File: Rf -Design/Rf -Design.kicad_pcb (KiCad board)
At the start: 4 copper layers, 39.8 x 17.2 mm, 39 parts, among them J1 USB_B_Micro, J2 SMA, J3 SWD, U1 XC6206PxxxMR, U2 USBLC6-2SC6, U3 STM32L432KBUx, U4 nRF24L01P, Y1 Crystal_GND23

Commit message: Update README.md
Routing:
- net +3V3: track 4.99 -> 11.5 mm

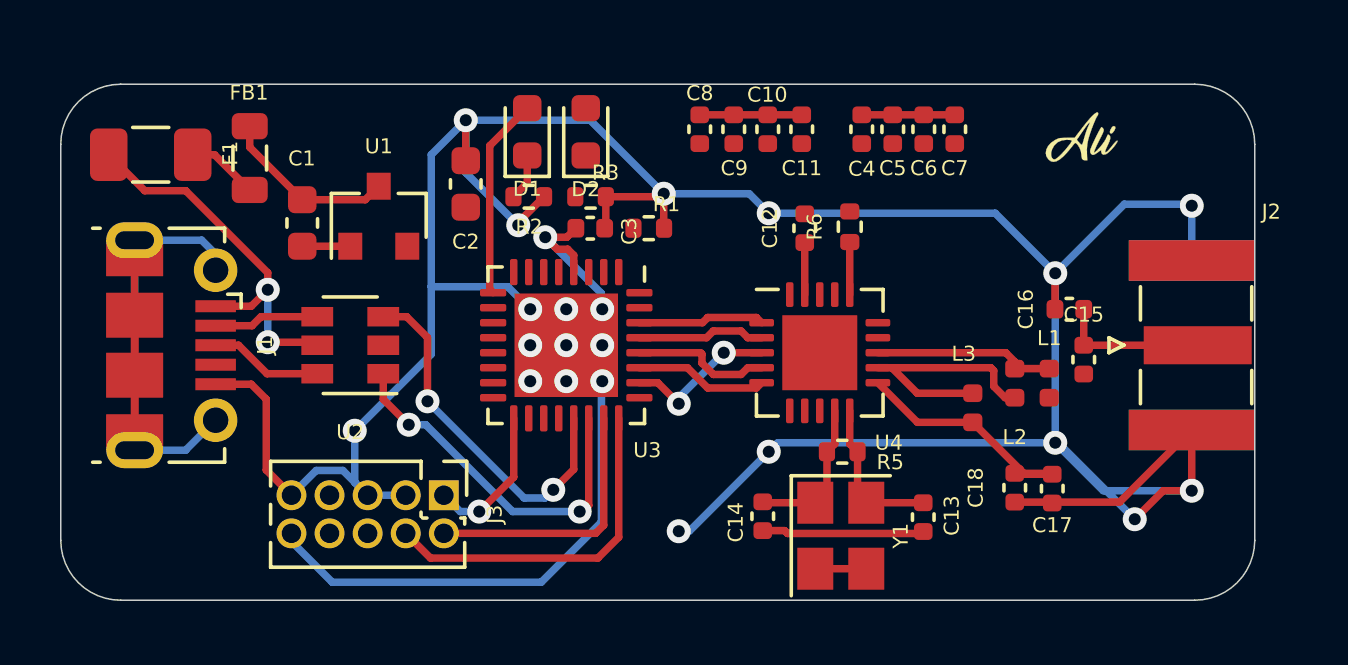
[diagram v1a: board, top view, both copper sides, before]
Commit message: Route tracks are arranged
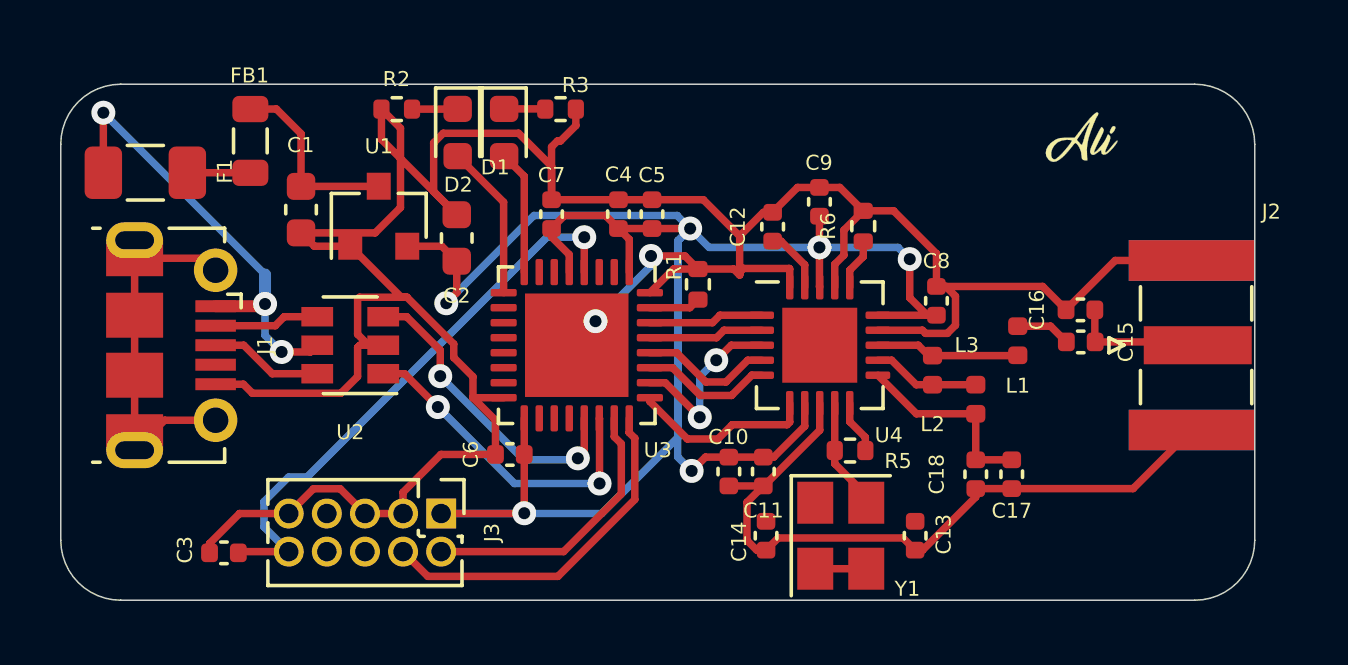
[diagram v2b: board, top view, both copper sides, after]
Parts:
- moved C6 17.5 mm to (110.4, 93.7), turned to 180 degrees
- moved C3 16.3 mm to (100.8, 97.0), turned to 180 degrees
- moved C7 13.7 mm to (111.8, 85.7), turned to 90 degrees
- moved C10 11.5 mm to (117.7, 94.3)
- moved C11 11.5 mm to (118.8, 94.3)
- moved C8 9.75 mm to (124.6, 88.6), turned to 90 degrees
- moved C4 8.59 mm to (114.0, 85.7), turned to 90 degrees
- moved C5 8.51 mm to (115.1, 85.7), turned to 90 degrees
- moved R2 5.28 mm to (106.6, 82.2), turned to 180 degrees
- moved C9 3.74 mm to (120.7, 85.3), turned to 90 degrees
- moved R3 3.09 mm to (112.1, 82.2)
- moved L2 2.77 mm to (124.5, 90.9)
- moved D2 2.72 mm to (110.2, 83.0), turned to 270 degrees
- moved R1 2.49 mm to (116.6, 88.1), turned to 90 degrees
- moved D1 2.32 mm to (108.6, 83.0), turned to 270 degrees
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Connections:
- Y1 pad 1: NRF_XC2 -> NRF_XC1
- Y1 pad 4: NRF_XC1 -> NRF_XC2
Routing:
- net +3V3: track 11.5 -> 71.3 mm, vias 1 -> 6
- net Net-(J1-Pad6): track 24.4 -> 13.0 mm
- net GND: track 117.4 -> 128.1 mm, vias 21 -> 2
- net NRF_IRQ: track 0.00 -> 6.16 mm
- net NRST: track 25.2 -> 19.2 mm
- net NRF_ANT1: track 8.33 -> 3.60 mm
- net Net-(D2-Pad2): track 0.00 -> 4.14 mm
- net NRF_XC1: track 5.19 -> 2.34 mm
- net +5V: track 12.9 -> 15.5 mm, vias 2 -> 3
- net Net-(C15-Pad1): track 0.00 -> 1.84 mm
- net NRF_VDD_PA: track 8.34 -> 6.53 mm
- net USB_D-: track 12.2 -> 10.4 mm
- net Net-(R1-Pad1): track 0.00 -> 1.71 mm
- net Net-(D1-Pad2): track 6.71 -> 5.19 mm
- net Net-(D2-Pad1): track 0.00 -> 1.37 mm
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- removed copper zone on In2.Cu, net +3V3

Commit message: The texts on the f-silk layer are fixed
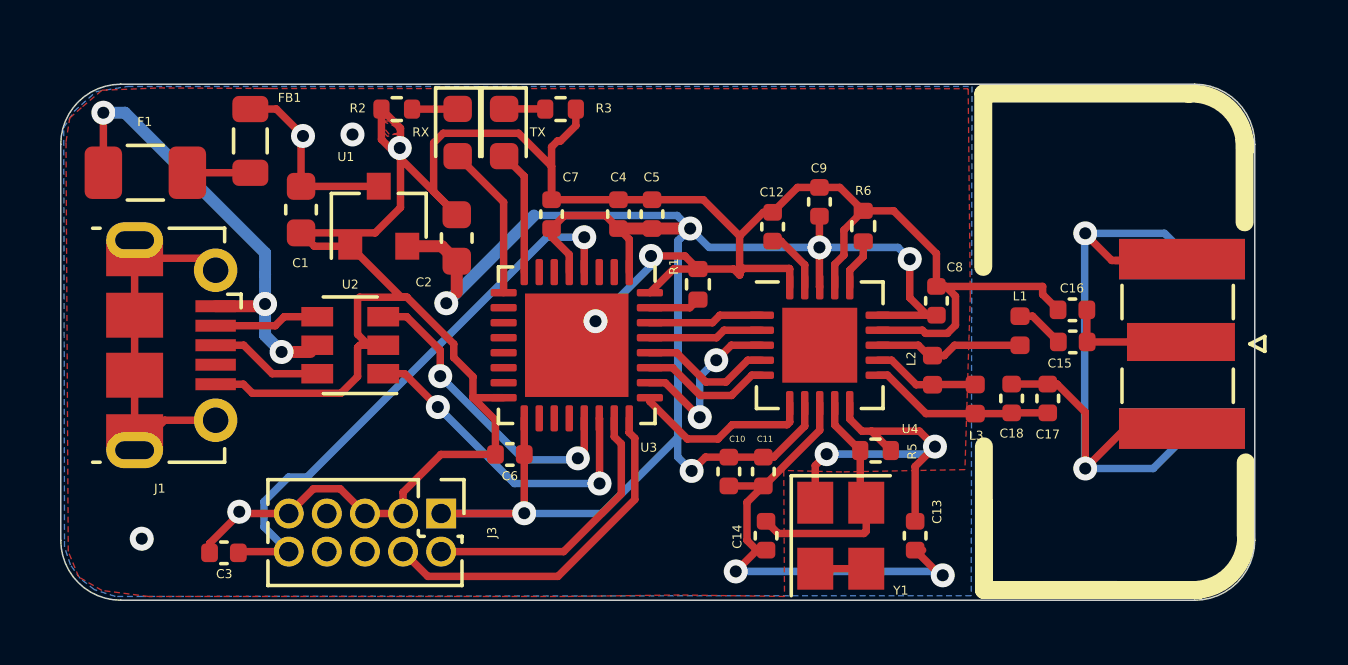
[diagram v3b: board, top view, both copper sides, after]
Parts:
- G***: moved to B.Cu
- moved G*** 12.0 mm to (117.5, 83.0)
- moved C17 2.80 mm to (128.3, 91.9), turned to 90 degrees
- moved C18 2.79 mm to (127.1, 91.9), turned to 90 degrees
- moved R5 0.85 mm to (122.6, 93.6)
- moved L1 0.34 mm to (127.4, 89.6)
- moved J2 0.33 mm to (132.8, 90.1), turned to 270 degrees
- moved C15 0.27 mm to (129.1, 90.0)
- moved C16 0.27 mm to (129.1, 88.9)
- renumbered D1 to RX, D2 to TX
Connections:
- C1 pad 1: Net-(C1-Pad1) -> GND
- FB1 pad 1: Net-(C1-Pad1) -> GND
- U1 pad 3: Net-(C1-Pad1) -> GND
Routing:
- net GND: track 128.1 -> 154.1 mm, vias 2 -> 11
- net NRF_XC1: track 2.34 -> 13.5 mm, vias 0 -> 2
- net Net-(C1-Pad1): track 6.38 -> 0.00 mm
- net NRF_XC2: track 4.16 -> 8.90 mm
- added copper zone on In2.Cu, net +3V3
- added copper zone on B.Cu, net GND
- added copper zone on F.Cu, net GND
